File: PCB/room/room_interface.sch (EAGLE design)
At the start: 31 parts

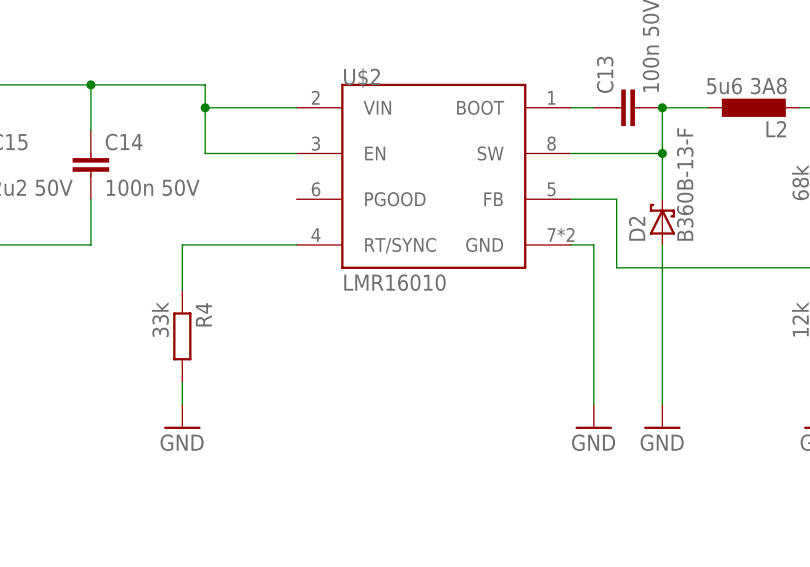
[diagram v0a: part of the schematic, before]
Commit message: finished routing for room sensor PCB
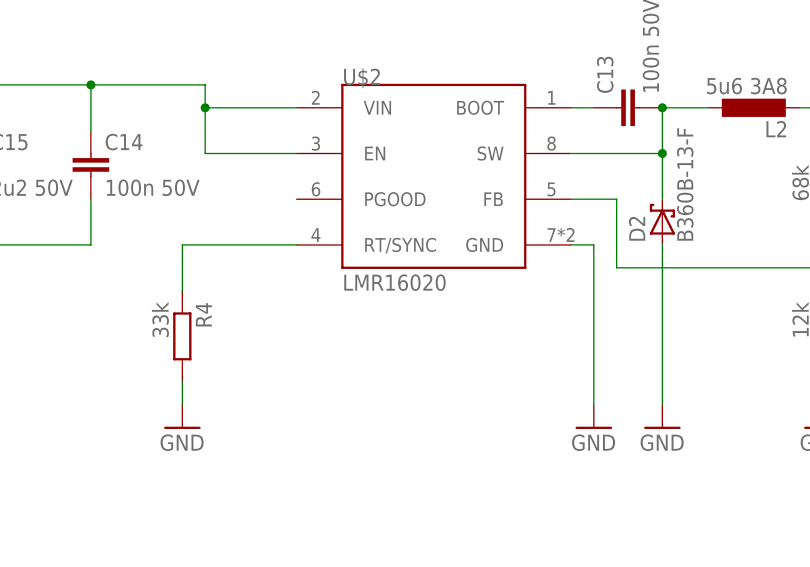
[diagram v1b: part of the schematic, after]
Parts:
- U$2: value LMR16010 -> LMR16020; device LMR160X0_snapEDA:LMR16010 -> LMR160X0_snapEDA:LMR16020
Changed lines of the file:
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@@
 <grid distance="0.1" unitdist="inch" unit="inch" style="lines" multiple="1" display="no" altdistance="0.01" altunitdist="inch" altunit="inch"/>
 <layers>
-<layer number="1" name="Top" color="4" fill="1" visible="no" active="no"/>
-<layer number="2" name="Route2" color="1" fill="3" visible="no" active="no"/>
-<layer number="3" name="Route3" color="4" fill="3" visible="no" active="no"/>
-<layer number="4" name="Route4" color="1" fill="4" visible="no" active="no"/>
-<layer number="5" name="Route5" color="4" fill="4" visible="no" active="no"/>
-<layer number="6" name="Route6" color="1" fill="8" visible="no" active="no"/>
-<layer number="7" name="Route7" color="4" fill="8" visible="no" active="no"/>
-<layer number="8" name="Route8" color="1" fill="2" visible="no" active="no"/>
-<layer number="9" name="Route9" color="4" fill="2" visible="no" active="no"/>
-<layer number="10" name="Route10" color="1" fill="7" visible="no" active="no"/>
-<layer number="11" name="Route11" color="4" fill="7" visible="no" active="no"/>
-<layer number="12" name="Route12" color="1" fill="5" visible="no" active="no"/>
-<layer number="13" name="Route13" color="4" fill="5" visible="no" active="no"/>
-<layer number="14" name="Route14" color="1" fill="6" visible="no" active="no"/>
-<layer number="15" name="Route15" color="4" fill="6" visible="no" active="no"/>
-<layer number="16" name="Bottom" color="1" fill="1" visible="no" active="no"/>
-<layer number="17" name="Pads" color="2" fill="1" visible="no" active="no"/>
-<layer number="18" name="Vias" color="2" fill="1" visible="no" active="no"/>
-<layer number="19" name="Unrouted" color="6" fill="1" visible="no" active="no"/>
-<layer number="20" name="Dimension" color="15" fill="1" visible="no" active="no"/>
-<layer number="21" name="tPlace" color="7" fill="1" visible="no" active="no"/>
-<layer number="22" name="bPlace" color="7" fill="1" visible="no" active="no"/>
-<layer number="23" name="tOrigins" color="15" fill="1" visible="no" active="no"/>
-<layer number="24" name="bOrigins" color="15" fill="1" visible="no" active="no"/>
-<layer number="25" name="tNames" color="7" fill="1" visible="no" active="no"/>
-<layer number="26" name="bNames" color="7" fill="1" visible="no" active="no"/>
-<layer number="27" name="tValues" color="7" fill="1" visible="no" active="no"/>
-<layer number="28" name="bValues" color="7" fill="1" visible="no" active="no"/>
+<layer number="1" name="Top" color="4" fill="1" visible="yes" active="no"/>
+<layer number="2" name="Route2" color="1" fill="3" visible="yes" active="no"/>
+<layer number="3" name="Route3" color="4" fill="3" visible="yes" active="no"/>
+<layer number="4" name="Route4" color="1" fill="4" visible="yes" active="no"/>
+<layer number="5" name="Route5" color="4" fill="4" visible="yes" active="no"/>
+<layer number="6" name="Route6" color="1" fill="8" visible="yes" active="no"/>
+<layer number="7" name="Route7" color="4" fill="8" visible="yes" active="no"/>
+<layer number="8" name="Route8" color="1" fill="2" visible="yes" active="no"/>
+<layer number="9" name="Route9" color="4" fill="2" visible="yes" active="no"/>
+<layer number="10" name="Route10" color="1" fill="7" visible="yes" active="no"/>
+<layer number="11" name="Route11" color="4" fill="7" visible="yes" active="no"/>
+<layer number="12" name="Route12" color="1" fill="5" visible="yes" active="no"/>
+<layer number="13" name="Route13" color="4" fill="5" visible="yes" active="no"/>
+<layer number="14" name="Route14" color="1" fill="6" visible="yes" active="no"/>
+<layer number="15" name="Route15" color="4" fill="6" visible="yes" active="no"/>
+<layer number="16" name="Bottom" color="1" fill="1" visible="yes" active="no"/>
+<layer number="17" name="Pads" color="2" fill="1" visible="yes" active="no"/>
+<layer number="18" name="Vias" color="2" fill="1" visible="yes" active="no"/>
+<layer number="19" name="Unrouted" color="6" fill="1" visible="yes" active="no"/>
+<layer number="20" name="Dimension" color="15" fill="1" visible="yes" active="no"/>
+<layer number="21" name="tPlace" color="7" fill="1" visible="yes" active="no"/>
+<layer number="22" name="bPlace" color="7" fill="1" visible="yes" active="no"/>
+<layer number="23" name="tOrigins" color="15" fill="1" visible="yes" active="no"/>
+<layer number="24" name="bOrigins" color="15" fill="1" visible="yes" active="no"/>
+<layer number="25" name="tNames" color="7" fill="1" visible="yes" active="no"/>
+<layer number="26" name="bNames" color="7" fill="1" visible="yes" active="no"/>
+<layer number="27" name="tValues" color="7" fill="1" visible="yes" active="no"/>
+<layer number="28" name="bValues" color="7" fill="1" visible="yes" active="no"/>
 <layer number="29" name="tStop" color="7" fill="3" visible="no" active="no"/>
 <layer number="30" name="bStop" color="7" fill="6" visible="no" active="no"/>
@@
 <layer number="35" name="tGlue" color="7" fill="4" visible="no" active="no"/>
 <layer number="36" name="bGlue" color="7" fill="5" visible="no" active="no"/>
-<layer number="37" name="tTest" color="7" fill="1" visible="no" active="no"/>
-<layer number="38" name="bTest" color="7" fill="1" visible="no" active="no"/>
+<layer number="37" name="tTest" color="7" fill="1" visible="yes" active="no"/>
+<layer number="38" name="bTest" color="7" fill="1" visible="yes" active="no"/>
 <layer number="39" name="tKeepout" color="4" fill="11" visible="no" active="no"/>
 <layer number="40" name="bKeepout" color="1" fill="11" visible="no" active="no"/>
@@
 <layer number="44" name="Drills" color="7" fill="1" visible="no" active="no"/>
 <layer number="45" name="Holes" color="7" fill="1" visible="no" active="no"/>
-<layer number="46" name="Milling" color="3" fill="1" visible="no" active="no"/>
-<layer number="47" name="Measures" color="7" fill="1" visible="no" active="no"/>
-<layer number="48" name="Document" color="7" fill="1" visible="no" active="no"/>
-<layer number="49" name="Reference" color="7" fill="1" visible="no" active="no"/>
-<layer number="50" name="dxf" color="7" fill="1" visible="no" active="no"/>
-<layer number="51" name="tDocu" color="7" fill="1" visible="no" active="no"/>
-<layer number="52" name="bDocu" color="7" fill="1" visible="no" active="no"/>
-<layer number="53" name="tGND_GNDA" color="7" fill="9" visible="no" active="no"/>
-<layer number="54" name="bGND_GNDA" color="1" fill="9" visible="no" active="no"/>
-<layer number="56" name="wert" color="7" fill="1" visible="no" active="no"/>
+<layer number="46" name="Milling" color="3" fill="1" visible="yes" active="no"/>
+<layer number="47" name="Measures" color="7" fill="1" visible="yes" active="no"/>
+<layer number="48" name="Document" color="7" fill="1" visible="yes" active="no"/>
+<layer number="49" name="Reference" color="7" fill="1" visible="yes" active="no"/>
+<layer number="50" name="dxf" color="7" fill="1" visible="yes" active="no"/>
+<layer number="51" name="tDocu" color="7" fill="1" visible="yes" active="no"/>
+<layer number="52" name="bDocu" color="7" fill="1" visible="yes" active="no"/>
+<layer number="53" name="tGND_GNDA" color="7" fill="9" visible="yes" active="no"/>
+<layer number="54" name="bGND_GNDA" color="1" fill="9" visible="yes" active="no"/>
+<layer number="56" name="wert" color="7" fill="1" visible="yes" active="no"/>
 <layer number="90" name="Modules" color="5" fill="1" visible="yes" active="yes"/>
 <layer number="91" name="Nets" color="2" fill="1" visible="yes" active="yes"/>
@@
 <part name="C8" library="rcl" deviceset="C-EU" device="C1206" value="2u2 50V"/>
 <part name="GND6" library="supply1" deviceset="GND" device=""/>
-<part name="U$2" library="LMR160X0_snapEDA" deviceset="LMR16010" device=""/>
+<part name="U$2" library="LMR160X0_snapEDA" deviceset="LMR16020" device=""/>
 <part name="R4" library="rcl" deviceset="R-EU_" device="R1206" value="33k"/>
 <part name="GND7" library="supply1" deviceset="GND" device=""/>

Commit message: finished interface PCB
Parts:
- removed C10: 1uF 16V, rcl:C-EUC0805
- removed C11, C12: 47u 10V, rcl:C-EUC1210
- removed C13, C14, C5, C6: 100n 50V, rcl:C-EUC1206
- removed C15, C16, C7, C8: 2u2 50V, rcl:C-EUC1206
- removed C17, C18: (no value), rcl:CPOL-EUUD-5X5,8
- removed C4: 22u 16V, rcl:C-EUC1210
- removed C9: NM, rcl:C-EUC1206
- removed D1: B260-13-F, diode:MBRS130LT3
- removed D2: B360B-13-F, diode:MBRS130LT3
- removed L1: 15u 2A2, parts:SLF10145T-150M2R2-PF
- removed L2: 5u6 3A8, parts:SLF10145T-150M2R2-PF
- removed U$1: LMR16010, LMR160X0_snapEDA:LMR16010
- removed U$2: LMR16020, LMR160X0_snapEDA:LMR16020
- added CON1, CON2: XG4H-1431, parts:XG4H-1431
- added D5: B260-13-F, diode:MBRS130LT3
- added F1, F2, F3, F4: 40012000000, 400XXX0000:40012000000
- added LOGO1: OSHW_LOGO_FILLX0350-NT, ohw-logo:OSHW_LOGO_FILLX0350-NT
- added OK1, OK2, OK3: SFH6206, optocoupler:SFH6206
- added Q1, Q2, Q3, Q4, Q5, Q6: MMBTA06LT1G, transistor-npn:BC849SMD
- added R10, R8, R9: 100k 1W, rcl:R-EU_R2010
- added R11, R12, R13, R15, R18, R21: 10k, rcl:R-EU_R1206
- added R14, R17, R20: 100k, rcl:R-EU_R1206
- added R16, R19, R22: 100R, rcl:R-EU_R1206
- added T1, T2, T3, T4: WJ500V-5.08-3P, parts:WJ500V-5.08-3P
- added T5, T6, T7, T8: WJ142R-5.08-2P, parts:WJ142R-5.08-2P
- added V1, V2, V3: B72205S0251K101, varistor:S05K250
- added X1: (no value), con-phoenix-254:MPT4
- C1: value 1uF 16V -> 1u 16V
- C2: value 22u 16V -> 1u 16V; device rcl:C-EUC1210 -> rcl:C-EUC0805
- C3: value NM -> 1u 16V; device rcl:C-EUC1206 -> rcl:C-EUC0805
- R1: value 33k -> G3MB202PDC24; device rcl:R-EU_R1206 -> RELAY_G3MB202PDC5_snapEDA:RELAY_G3MB202PDC5
- R2: value 12k -> G3MB202PDC24; device rcl:R-EU_R1206 -> RELAY_G3MB202PDC5_snapEDA:RELAY_G3MB202PDC5
- R3: value 68k -> G3MB202PDC24; device rcl:R-EU_R1206 -> RELAY_G3MB202PDC5_snapEDA:RELAY_G3MB202PDC5
- R4: value 33k -> B72214S0300K101; device rcl:R-EU_R1206 -> varistor:S14K300
- R5: value 12k -> 100k 1W; device rcl:R-EU_R1206 -> rcl:R-EU_R2010
- R6: value 68k -> 100k 1W; device rcl:R-EU_R1206 -> rcl:R-EU_R2010
- R7: value 100k -> 100k 1W; device rcl:R-EU_R1206 -> rcl:R-EU_R2010
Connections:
- removed net +5V: C1.1, C2.1, C3.1, C4.1, L1.2, R3.1
- new net A0: CON2.1, T1.1
- new net A1: CON2.3, T1.3
- new net A2: CON2.5, T3.1
- new net A3: CON2.7, T3.3
- new net B0: CON2.2, T1.2
- new net B1: CON2.4, T2.1
- new net B2: CON2.6, T3.2
- new net B3: CON2.8, T4.1
- new net ESP32_IO1: CON2.9
- new net ESP32_IO12: CON2.11
- new net ESP32_IO13: CON2.13
- new net ESP32_IO14: CON2.12
- new net ESP32_IO15: CON2.14
- new net ESP32_IO3: CON2.10
- new net IN1: R5.1, T5.1
- new net IN2: R7.1, T6.1
- new net IN3: R9.1, T7.1
- new net IO0: CON1.5, R11.1
- new net IO1: CON1.6, R12.1
- new net IO2: CON1.7, R13.1
- new net IO3: CON1.8
- new net IO4: CON1.9
- new net IO5: CON1.10, Q4.C, R15.1
- new net IO6: CON1.11, Q5.C, R18.1
- new net IO7: CON1.12, Q6.C, R21.1
- new net LIVE: R1.OUT2, R2.OUT2, R3.OUT2, T8.2, V1.1, V2.1, V3.1
- new net N$11: OK3.AC2, R10.2
- new net N$12: Q1.B, R11.2
- new net N$13: Q1.C, R1.IN-
- new net N$15: Q2.B, R12.2
- new net N$16: Q2.C, R2.IN-
- new net N$17: Q4.B, R14.2
- new net N$18: Q3.B, R13.2
- new net N$19: Q3.C, R3.IN-
- new net N$20: OK1.E, R16.1
- new net N$21: C1.1, R14.1, R16.2
- new net N$23: Q5.B, R17.2
- new net N$24: OK2.E, R19.1
- new net N$25: C2.1, R17.1, R19.2
- new net N$27: Q6.B, R20.2
- new net N$28: OK3.E, R22.1
- new net N$29: C3.1, R20.1, R22.2
- new net N$5: OK1.AC2, R6.2
- new net N$6: F4.1, T2.3, T4.3
- new net NEUTRAL: R10.1, R6.1, R8.1, T8.1
- new net OUT1: F1.2, T5.2
- new net OUT2: F2.2, T6.2
- new net OUT3: F3.2, T7.2
- new net SDA: CON1.14, X1-2.1
- new net SDC: CON1.13, X1-3.1
- net +24V: now also CON1.2, D5.C, R1.IN+, R2.IN+, R3.IN+; no longer C14.1, C15.1, C16.1, C17.+, C18.+, C6.1, C7.1, C8.1, U$1.EN, U$1.VIN, U$2.EN, U$2.VIN
- net +3V3: now also CON1.4, OK1.C, OK2.C, OK3.C, R15.2, R18.2, R21.2, X1-1.1; no longer C10.1, C11.1, C12.1, C9.1, L2.2, R6.1, R7.1
- net GND: now also C3.2, CON1.1, CON1.3, Q1.E, Q2.E, Q3.E, Q4.E, Q5.E, Q6.E, R4.1, T2.2, T4.2, X1-4.1; no longer C10.2, C11.2, C12.2, C14.2, C15.2, C16.2, C17.-, C18.-, C4.2, C6.2, C7.2, C8.2, D1.A, D2.A, R1.2, R2.2, R4.2, R5.2, U$1.GND, U$2.GND
- net N$1: now also F1.1, R1.OUT1, V1.2; no longer C5.2, D1.C, L1.1, U$1.SW
- net N$10: now also OK3.AC1, R9.2; no longer C13.1, U$2.BOOT
- net N$2: now also F2.1, R2.OUT1, V2.2; no longer R1.1, U$1.RT/SYNC
- net N$3: now also F3.1, R3.OUT1, V3.2; no longer C3.2, R2.1, R3.2, U$1.FB
- net N$4: now also D5.A, F4.2, R4.2; no longer C5.1, U$1.BOOT
- net N$7: now also OK1.AC1, R5.2; no longer R4.1, U$2.RT/SYNC
- net N$8: now also OK2.AC1; no longer C9.2, R5.1, R6.2, U$2.FB
- net N$9: now also OK2.AC2, R8.2; no longer C13.2, D2.C, L2.1, U$2.SW
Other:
- note added: "CONNECTOR"
- note added: "INPUTS"
- note added: "OUTPUTS"
- note added: "TERMINALS"
